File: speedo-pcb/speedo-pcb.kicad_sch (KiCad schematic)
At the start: 57 parts, among them J1 Debug, J2 Mode, J3 Speedo, J4 Power, J5 VBAT, J6 BOOT, J7 Breakout, M1 X27_128, U1 XC6206P332MR, U3 OLED_128x32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

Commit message: change tvs
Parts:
- removed D14: P6SMB6.8CA/TR13, PCM_JLCPCB:D_SMB, symbol PCM_JLCPCB-Diodes:TVS-Bi,P6SMB6.8CA/TR13
- added D10: SMAJ16A, PCM_JLCPCB:D_SMA, symbol PCM_JLCPCB-Diodes:TVS-Uni,SMAJ16A
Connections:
- net +12V: now also D10.1
- net GND: now also D10.2
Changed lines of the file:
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@@
 	)
 	(symbol
+		(lib_id "PCM_JLCPCB-Diodes:TVS-Uni,SMAJ16A")
+		(at 36.83 34.29 180)
+		(unit 1)
+		(exclude_from_sim no)
+		(in_bom yes)
+		(on_board yes)
+		(dnp no)
+		(fields_autoplaced yes)
+		(property "Reference" "D10"
+			(at 41.91 32.7024 0)
+			(effects
+				(font
+					(size 1.27 1.27)
+				)
+				(justify right)
+			)
+		)
+		(property "Value" "SMAJ16A"
+			(at 41.91 35.2425 0)
+			(effects
+				(font
+					(size 0.8 0.8)
+				)
+				(justify right)
+			)
+		)
+		(property "Footprint" "PCM_JLCPCB:D_SMA"
+			(at 38.608 34.29 90)
+			(effects
+				(font
+					(size 1.27 1.27)
+				)
+				(hide yes)
+			)
+		)
+		(property "Datasheet" "https://www.lcsc.com/datasheet/lcsc_datasheet_2411041728_hongjiacheng-SMAJ16A_C41376405.pdf"
+			(at 36.83 34.29 0)
+			(effects
+				(font
+					(size 1.27 1.27)
+				)
+				(hide yes)
+			)
+		)
+		(property "Description" "26V 400W 19.7V Unidirectional 16V SMA ESD and Surge Protection (TVS/ESD) ROHS"
+			(at 36.83 34.29 0)
+			(effects
+				(font
+					(size 1.27 1.27)
+				)
+				(hide yes)
+			)
+		)
+		(property "LCSC" "C41376405"
+			(at 36.83 34.29 0)
+			(effects
+				(font
+					(size 1.27 1.27)
+				)
+				(hide yes)
+			)
+		)
+		(property "Stock" "11587"
+			(at 36.83 34.29 0)
+			(effects
+				(font
+					(size 1.27 1.27)
+				)
+				(hide yes)
+			)
+		)
+		(property "Price" "0.038USD"
+			(at 36.83 34.29 0)
+			(effects
+				(font
+					(size 1.27 1.27)
+				)
+				(hide yes)
+			)
+		)
+		(property "Process" "SMT"
+			(at 36.83 34.29 0)
+			(effects
+				(font
+					(size 1.27 1.27)
+				)
+				(hide yes)
+			)
+		)
+		(property "Minimum Qty" "5"
+			(at 36.83 34.29 0)
+			(effects
+				(font
+					(size 1.27 1.27)
+				)
+				(hide yes)
+			)
+		)
+		(property "Attrition Qty" "4"
+			(at 36.83 34.29 0)
+			(effects
+				(font
+					(size 1.27 1.27)
+				)
+				(hide yes)
+			)
+		)
+		(property "Class" "Preferred Component"
+			(at 36.83 34.29 0)
+			(effects
+				(font
+					(size 1.27 1.27)
+				)
+				(hide yes)
+			)
+		)
+		(property "Category" "Circuit Protection,ESD And Surge Protection (TVS/ESD)"
+			(at 36.83 34.29 0)
+			(effects
+				(font
+					(size 1.27 1.27)
+				)
+				(hide yes)
+			)
+		)
+		(property "Manufacturer" "hongjiacheng"
+			(at 36.83 34.29 0)
+			(effects
+				(font
+					(size 1.27 1.27)
+				)
+				(hide yes)
+			)
+		)
+		(property "Part" "SMAJ16A"
+			(at 36.83 34.29 0)
+			(effects
+				(font
+					(size 1.27 1.27)
+				)
+				(hide yes)
+			)
+		)
+		(property "Operating Temperature" "-55°C~+155°C"
+			(at 36.83 34.29 0)
+			(effects
+				(font
+					(size 1.27 1.27)
+				)
+				(hide yes)
+			)
+		)
+		(property "Type" "TVS"
+			(at 36.83 34.29 0)
+			(effects
+				(font
+					(size 1.27 1.27)
+				)
+				(hide yes)
+			)
+		)
+		(property "Peak Pulse Power Dissipation (Ppp)" "400W"
+			(at 36.83 34.29 0)
+			(effects
+				(font
+					(size 1.27 1.27)
+				)
+				(hide yes)
+			)
+		)
+		(property "Number of Lines" "Single channel"
+			(at 36.83 34.29 0)
+			(effects
+				(font
+					(size 1.27 1.27)
+				)
+				(hide yes)
+			)
+		)
+		(property "Breakdown Voltage" "19.7V"
+			(at 36.83 34.29 0)
+			(effects
+				(font
+					(size 1.27 1.27)
+				)
+				(hide yes)
+			)
+		)
+		(property "Maximum Clamping Voltage" "26V"
+			(at 36.83 34.29 0)
+			(effects
+				(font
+					(size 1.27 1.27)
+				)
+				(hide yes)
+			)
+		)
+		(property "Reverse Stand-Off Voltage (Vrwm)" "16V"
+			(at 36.83 34.29 0)
+			(effects
+				(font
+					(size 1.27 1.27)
+				)
+				(hide yes)
+			)
+		)
+		(property "Reverse Leakage Current (Ir)" "1uA"
+			(at 36.83 34.29 0)
+			(effects
+				(font
+					(size 1.27 1.27)
+				)
+				(hide yes)
+			)
+		)
+		(property "polarity" "Unidirectional"
+			(at 36.83 34.29 0)
+			(effects
+				(font
+					(size 1.27 1.27)
+				)
+				(hide yes)
+			)
+		)
+		(pin "2"
+		)
+		(pin "1"
+		)
+		(instances
+			(project ""
+				(path "/f54762c2-a8cc-4b58-9422-701295b95b42"
+					(reference "D10")
+					(unit 1)
+				)
+			)
+		)
+	)
+	(symbol
 		(lib_id "power:+3.3V")
 		(at 128.27 71.12 0)
@@
 					(unit 1)
 				)
-			)
-		)
-	)
-	(symbol
-		(lib_id "PCM_JLCPCB-Diodes:TVS-Bi,P6SMB6.8CA/TR13")
-		(at 36.83 34.29 0)
-		(unit 1)
-		(exclude_from_sim no)
-		(in_bom yes)
-		(on_board yes)
-		(dnp no)
-		(fields_autoplaced yes)
-		(property "Reference" "D14"
-			(at 41.91 33.0199 0)
-			(effects
-				(font
-					(size 1.27 1.27)
-				)
-				(justify left)
-			)
-		)
-		(property "Value" "P6SMB6.8CA/TR13"
-			(at 41.91 35.56 0)
-			(effects
-				(font
-					(size 0.8 0.8)
-				)
-				(justify left)
-			)
-		)
-		(property "Footprint" "PCM_JLCPCB:D_SMB"
-			(at 35.052 34.29 90)
-			(effects
-				(font
-					(size 1.27 1.27)
-				)
-				(hide yes)
-			)
-		)
-		(property "Datasheet" "https://www.lcsc.com/datasheet/lcsc_datasheet_1810181007_Brightking-P6SMB6-8CA-TR13_C78395.pdf"
-			(at 36.83 34.29 0)
-			(effects
-				(font
-					(size 1.27 1.27)
-				)
-				(hide yes)
-			)
-		)
-		(property "Description" "58.1A 600W 10.5V 6.45V 5.8V SMB(DO-214AA) ESD and Surge Protection (TVS/ESD) ROHS"
-			(at 36.83 34.29 0)
-			(effects
-				(font
-					(size 1.27 1.27)
-				)
-				(hide yes)
-			)
-		)
-		(property "LCSC" "C78395"
-			(at 36.83 34.29 0)
-			(effects
-				(font
-					(size 1.27 1.27)
-				)
-				(hide yes)
-			)
-		)
-		(property "Stock" "191189"
-			(at 36.83 34.29 0)
-			(effects
-				(font
-					(size 1.27 1.27)
-				)
-				(hide yes)
-			)
-		)
-		(property "Price" "0.050USD"
-			(at 36.83 34.29 0)
-			(effects
-				(font
-					(size 1.27 1.27)
-				)
-				(hide yes)
-			)
-		)
-		(property "Process" "SMT"
-			(at 36.83 34.29 0)
-			(effects
-				(font
-					(size 1.27 1.27)
-				)
-				(hide yes)
-			)
-		)
-		(property "Minimum Qty" "5"
-			(at 36.83 34.29 0)
-			(effects
-				(font
-					(size 1.27 1.27)
-				)
-				(hide yes)
-			)
-		)
-		(property "Attrition Qty" "4"
-			(at 36.83 34.29 0)
-			(effects
-				(font
-					(size 1.27 1.27)
-				)
-				(hide yes)
-			)
-		)
-		(property "Class" "Basic Component"
-			(at 36.83 34.29 0)
-			(effects
-				(font
-					(size 1.27 1.27)
-				)
-				(hide yes)
-			)
-		)
-		(property "Category" "Circuit Protection,TVS"
-			(at 36.83 34.29 0)
-			(effects
-				(font
-					(size 1.27 1.27)
-				)
-				(hide yes)
-			)
-		)
-		(property "Manufacturer" "Brightking Elec (TAIWAN)"
-			(at 36.83 34.29 0)
-			(effects
-				(font
-					(size 1.27 1.27)
-				)
-				(hide yes)
-			)
-		)
-		(property "Part" "P6SMB6.8CA/TR13"
-			(at 36.83 34.29 0)
-			(effects
-				(font
-					(size 1.27 1.27)
-				)
-				(hide yes)
-			)
-		)
-		(property "Bidirectional Channels" "1"
-			(at 36.83 34.29 0)
-			(effects
-				(font
-					(size 1.27 1.27)
-				)
-				(hide yes)
-			)
-		)
-		(property "Breakdown Voltage" "6.45V"
-			(at 36.83 34.29 0)
-			(effects
-				(font
-					(size 1.27 1.27)
-				)
-				(hide yes)
-			)
-		)
-		(property "Maximum Clamping Voltage" "10.5V"
-			(at 36.83 34.29 0)
-			(effects
-				(font
-					(size 1.27 1.27)
-				)
-				(hide yes)
-			)
-		)
-		(property "Reverse Stand-Off Voltage (Vrwm)" "5.8V"
-			(at 36.83 34.29 0)
-			(effects
-				(font
-					(size 1.27 1.27)
-				)
-				(hide yes)
-			)
-		)
-		(property "Peak Pulse Power Dissipation (Ppp)@10/1000us" "600W"
-			(at 36.83 34.29 0)
-			(effects
-				(font
-					(size 1.27 1.27)
-				)
-				(hide yes)
-			)
-		)
-		(property "Peak Pulse Current (Ipp)@10/1000us" "58.1A"
-			(at 36.83 34.29 0)
-			(effects
-				(font
-					(size 1.27 1.27)
-				)
-				(hide yes)
-			)
-		)
-		(pin "2"
-		)
-		(pin "1"
-		)
-		(instances
-			(project ""
-				(path "/f54762c2-a8cc-4b58-9422-701295b95b42"
-					(reference "D14")
-					(unit 1)
-				)

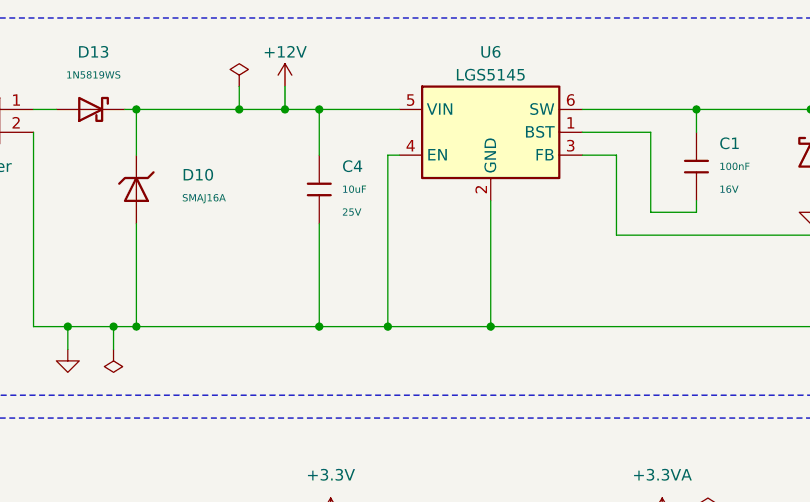
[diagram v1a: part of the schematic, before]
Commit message: fix buck en pin
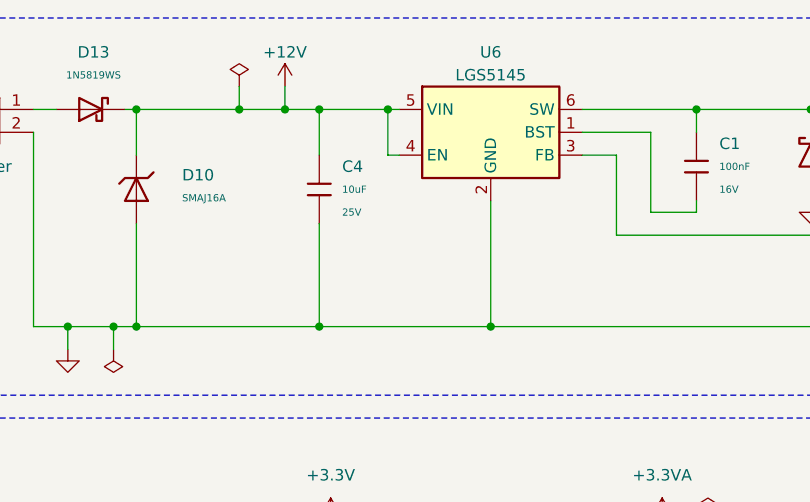
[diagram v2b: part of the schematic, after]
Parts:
- C10, C9: Stock 432692 -> 388678
- C11, C19, C2, C3, C7: Stock 28090188 -> 26683372
- C12: Stock 9266857 -> 8534728
- C13, C15: Stock 8425249 -> 7930855
- C14, C18: Stock 842329 -> 753654
- C8: Stock 2307117 -> 2112966
- D15: Stock 2351029 -> 2164219
- D9: Stock 952916 -> 882441
- FB1: Stock 475295 -> 460537
- R1: Stock 1000891 -> 981408
- R3: Stock 6919009 -> 5699128
- R5: Stock 671957 -> 613212
- R6: Stock 5578116 -> 5031445
- U4: Stock 156631 -> 226209
- X2: Stock 228988 -> 216941
- X3: Stock 313046 -> 304118
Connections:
- net +12V: now also U6.4 (EN)
- net GND: no longer U6.4 (EN)
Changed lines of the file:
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@@
 	)
 	(junction
-		(at 64.77 49.53)
-		(diameter 0)
-		(color 0 0 0 0)
-	)
-	(junction
 		(at 100.33 73.66)
 		(diameter 0)
@@
 	)
 	(junction
+		(at 64.77 25.4)
+		(diameter 0)
+		(color 0 0 0 0)
+	)
+	(junction
 		(at 248.92 124.46)
 		(diameter 0)
@@
 	(wire
 		(pts
+			(xy 64.77 25.4) (xy 66.04 25.4)
+		)
+		(stroke
+			(width 0)
+			(type default)
+		)
+	)
+	(wire
+		(pts
 			(xy 205.74 152.4) (xy 231.14 152.4)
 		)
@@
 	(wire
 		(pts
-			(xy 57.15 25.4) (xy 66.04 25.4)
+			(xy 57.15 25.4) (xy 64.77 25.4)
 		)
 		(stroke
@@
 	(wire
 		(pts
-			(xy 64.77 30.48) (xy 64.77 49.53)
-		)
-		(stroke
-			(width 0)
-			(type default)
-		)
-	)
-	(wire
-		(pts
 			(xy 35.56 73.66) (xy 24.13 73.66)
 		)
@@
 	(wire
 		(pts
+			(xy 64.77 25.4) (xy 64.77 30.48)
+		)
+		(stroke
+			(width 0)
+			(type default)
+		)
+	)
+	(wire
+		(pts
 			(xy 53.34 22.86) (xy 53.34 25.4)
 		)
@@
 	(wire
 		(pts
-			(xy 64.77 49.53) (xy 76.2 49.53)
-		)
-		(stroke
-			(width 0)
-			(type default)
-		)
-	)
-	(wire
-		(pts
 			(xy 187.96 134.62) (xy 190.5 134.62)
 		)
@@
 	(wire
 		(pts
-			(xy 57.15 49.53) (xy 64.77 49.53)
+			(xy 57.15 49.53) (xy 76.2 49.53)
 		)
 		(stroke
@@
 			)
 		)
-		(property "Stock" "9266857"
+		(property "Stock" "8534728"
 			(at 24.13 80.01 0)
 			(effects
@@
 			)
 		)
-		(property "Stock" "432692"
+		(property "Stock" "388678"
 			(at 26.67 118.11 0)
 			(effects
@@
 			)
 		)
-		(property "Stock" "156631"
+		(property "Stock" "226209"
 			(at 81.28 143.51 0)
 			(effects
@@
 	)
 	(symbol
+		(lib_name "Schottky,1N5819WS_2")
 		(lib_id "PCM_JLCPCB-Diodes:Schottky,1N5819WS")
 		(at 158.75 78.74 180)
@@
 			)
 		)
-		(property "Stock" "952916"
+		(property "Stock" "882441"
 			(at 158.75 78.74 0)
 			(effects
@@
 	)
 	(symbol
+		(lib_name "0402,1uF_1")
 		(lib_id "PCM_JLCPCB-Capacitors:0402,1uF")
 		(at 106.68 80.01 0)
@@
 			)
 		)
-		(property "Stock" "8425249"
+		(property "Stock" "7930855"
 			(at 106.68 80.01 0)
 			(effects
@@
 	)
 	(symbol
+		(lib_name "0402,51Ω_1")
 		(lib_id "PCM_JLCPCB-Resistors:0402,51Ω")
 		(at 251.46 85.09 0)
@@
 			)
 		)
-		(property "Stock" "1000891"
+		(property "Stock" "981408"
 			(at 251.46 85.09 0)
 			(effects
@@
 			)
 		)
-		(property "Stock" "842329"
+		(property "Stock" "753654"
 			(at 33.02 156.21 0)
 			(effects
@@
 			)
 		)
-		(property "Stock" "6919009"
+		(property "Stock" "5699128"
 			(at 39.37 104.14 0)
 			(effects
@@
 	)
 	(symbol
+		(lib_name "0402,1uF_2")
 		(lib_id "PCM_JLCPCB-Capacitors:0402,1uF")
 		(at 128.27 80.01 0)
@@
 			)
 		)
-		(property "Stock" "8425249"
+		(property "Stock" "7930855"
 			(at 128.27 80.01 0)
 			(effects
@@
 	)
 	(symbol
+		(lib_name "0402,100nF_4")
 		(lib_id "PCM_JLCPCB-Capacitors:0402,100nF")
 		(at 58.42 80.01 0)
@@
 			)
 		)
-		(property "Stock" "28090188"
+		(property "Stock" "26683372"
 			(at 58.42 80.01 0)
 			(effects
@@
 			)
 		)
-		(property "Stock" "28090188"
+		(property "Stock" "26683372"
 			(at 158.75 91.44 0)
 			(effects
@@
 			)
 		)
-		(property "Stock" "313046"
+		(property "Stock" "304118"
 			(at 35.56 128.27 0)
 			(effects
@@
 			)
 		)
-		(property "Stock" "2307117"
+		(property "Stock" "2112966"
 			(at 95.25 80.01 0)
 			(effects
@@
 	)
 	(symbol
+		(lib_name "0402,100nF_2")
 		(lib_id "PCM_JLCPCB-Capacitors:0402,100nF")
 		(at 35.56 80.01 0)
@@
 			)
 		)
-		(property "Stock" "28090188"
+		(property "Stock" "26683372"
 			(at 35.56 80.01 0)
 			(effects
@@
 	)
 	(symbol
+		(lib_name "0402,10pF_1")
 		(lib_id "PCM_JLCPCB-Capacitors:0402,10pF")
 		(at 26.67 138.43 90)
@@
 			)
 		)
-		(property "Stock" "432692"
+		(property "Stock" "388678"
 			(at 26.67 138.43 0)
 			(effects
@@
 	)
 	(symbol
+		(lib_name "0402,100nF_3")
 		(lib_id "PCM_JLCPCB-Capacitors:0402,100nF")
 		(at 46.99 80.01 0)
@@
 			)
 		)
-		(property "Stock" "28090188"
+		(property "Stock" "26683372"
 			(at 46.99 80.01 0)
 			(effects
@@
 			)
 		)
-		(property "Stock" "671957"
+		(property "Stock" "613212"
 			(at 148.59 78.74 0)
 			(effects
@@
 			)
 		)
-		(property "Stock" "5578116"
+		(property "Stock" "5031445"
 			(at 148.59 91.44 0)
 			(effects
@@
 	)
 	(symbol
+		(lib_name "0402,100nF_5")
 		(lib_id "PCM_JLCPCB-Capacitors:0402,100nF")
 		(at 58.42 101.6 90)
@@
 			)
 		)
-		(property "Stock" "28090188"
+		(property "Stock" "26683372"
 			(at 58.42 101.6 0)
 			(effects
@@
 	)
 	(symbol
+		(lib_name "LED,0603,Red_1")
 		(lib_id "PCM_JLCPCB-Diodes:LED,0603,Red")
 		(at 251.46 77.47 0)
@@
 			)
 		)
-		(property "Stock" "2351029"
+		(property "Stock" "2164219"
 			(at 251.46 77.47 0)
 			(effects
@@
 			)
 		)
-		(property "Stock" "475295"
+		(property "Stock" "460537"
 			(at 119.38 73.66 0)
 			(effects
@@
 	)
 	(symbol
+		(lib_name "0402,15pF_1")
 		(lib_id "PCM_JLCPCB-Capacitors:0402,15pF")
 		(at 33.02 171.45 90)
@@
 			)
 		)
-		(property "Stock" "842329"
+		(property "Stock" "753654"
 			(at 33.02 171.45 0)
 			(effects
@@
 			)
 		)
-		(property "Stock" "228988"
+		(property "Stock" "216941"
 			(at 39.37 163.83 0)
 			(effects

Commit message: pcb cleanup
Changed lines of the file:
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@@
 		)
 		(property "Voltage Rated" "50V"
-			(at 28.7162 116.078 0)
+			(at 27.686 122.174 90)
 			(effects
 				(font
@@
 		)
 		(property "Voltage Rated" "16V"
-			(at 56.388 82.0562 0)
+			(at 55.626 82.55 0)
 			(effects
 				(font
@@
 		)
 		(property "Voltage Rated" "16V"
-			(at 33.782 83.312 0)
+			(at 33.274 82.804 0)
 			(effects
 				(font
@@
 		)
 		(property "Voltage Rated" "50V"
-			(at 28.7162 136.398 0)
+			(at 27.686 142.748 90)
 			(effects
 				(font
@@
 		)
 		(property "Voltage Rated" "16V"
-			(at 45.212 83.312 0)
+			(at 44.196 82.804 0)
 			(effects
 				(font
@@
 		(on_board yes)
 		(dnp no)
-		(fields_autoplaced yes)
 		(property "Reference" "#PWR030"
 			(at 35.56 104.14 0)
@@
 		)
 		(property "Value" "+3.3V"
-			(at 38.1 99.0599 0)
+			(at 32.512 96.266 0)
 			(effects
 				(font
@@
 		)
 		(property "Voltage Rated" "16V"
-			(at 60.4662 99.568 0)
+			(at 59.436 105.664 90)
 			(effects
 				(font
@@
 		)
 		(property "Current Rating" "800mA"
-			(at 120.9074 70.2564 0)
+			(at 121.158 77.978 90)
 			(effects
 				(font
